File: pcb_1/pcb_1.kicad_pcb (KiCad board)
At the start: 2 copper layers, 46 parts, among them J1 ACin, J2 Vout, J3 2N3055_conn, J4 DCin, P1 CONN_01X07, P2 CONN_01X01, P3 CONN_01X01, P4 CONN_01X01, P5 CONN_01X01, P6 CONN_01X01, P7 CONN_01X01, Q2 BD139, U1 MAX9944ASA+T, U2 MCP3422A0-E/SN, U3 MCP4822-E/SN, U4 INA213AIDCKT, U5 LM7705MM/NOPB, U6 SPX2920U-5.0, U7 25V_regulator, U8 op_amp, U9 INA240A1PWR

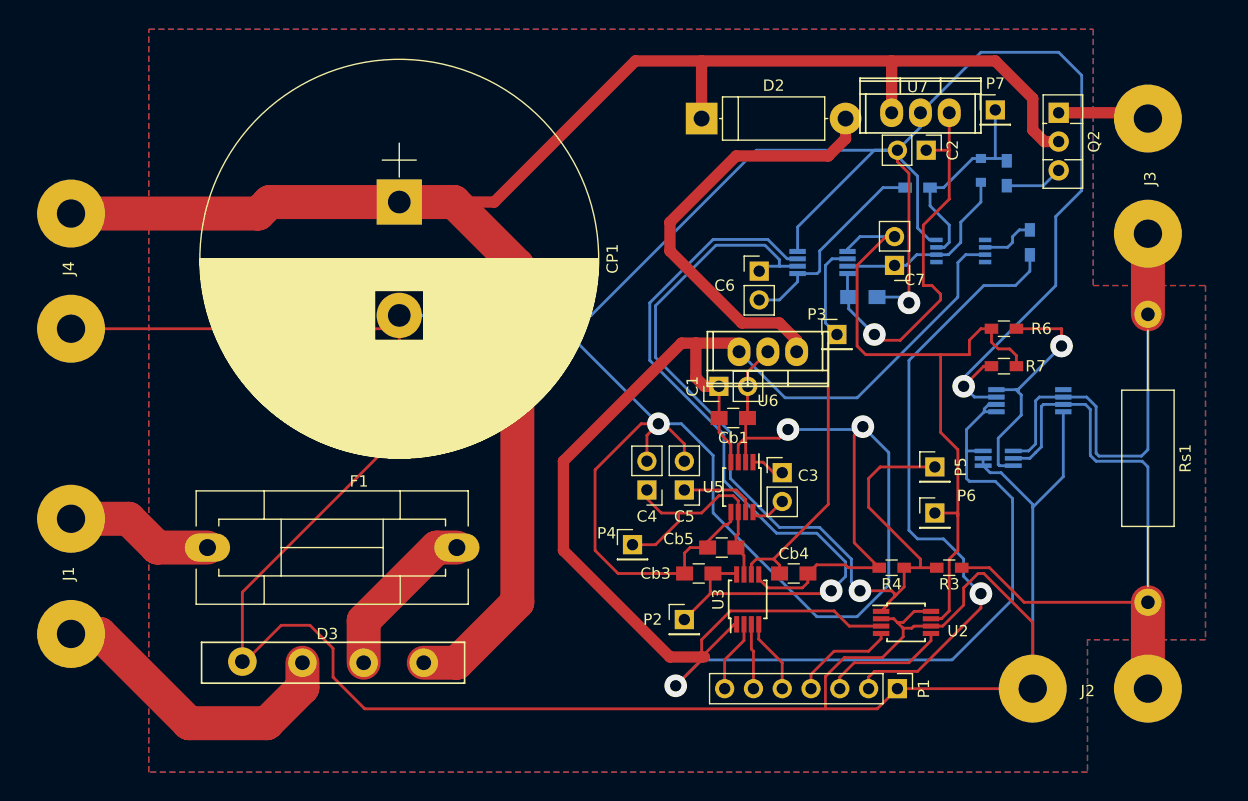
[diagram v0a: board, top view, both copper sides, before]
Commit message: Oparin regu vaihdettu ja konkkien footprintejä muutettu
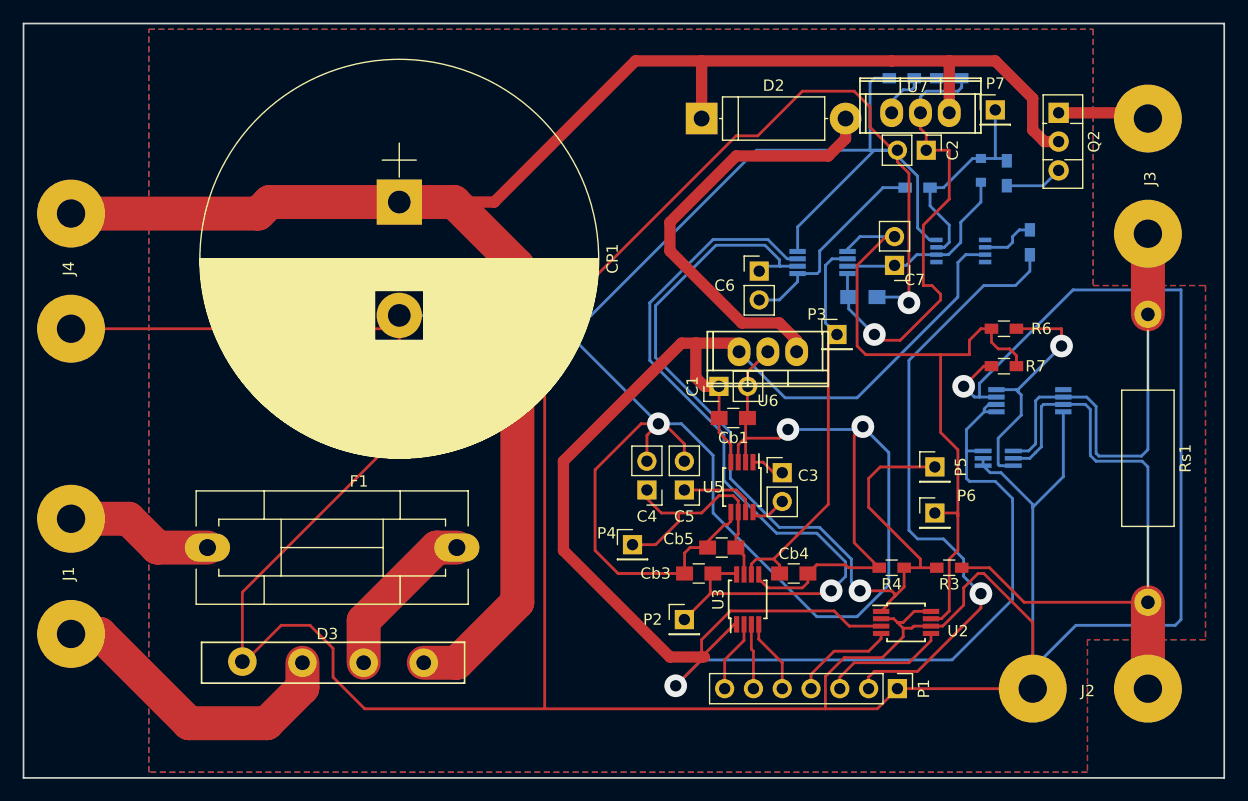
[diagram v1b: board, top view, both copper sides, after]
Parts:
- added R8: R, Resistors_SMD:R_0603_HandSoldering, B.Cu at (116.5, 33.0)
- added R9: R, Resistors_SMD:R_0603_HandSoldering, B.Cu at (120.7, 33.0)
- U7: value 25V_regulator -> LM317AT
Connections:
- U7 pad 1: Net-(CP1-Pad1) -> Net-(R8-Pad1)
- U7 pad 2: GND -> Net-(C2-Pad1)
- U7 pad 3: Net-(C2-Pad1) -> Net-(CP1-Pad1)
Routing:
- net GND: track 527.2 -> 627.0 mm
- net Net-(C2-Pad1): track 34.4 -> 40.9 mm
- net Net-(R8-Pad1): track 0.00 -> 6.31 mm
- net Net-(CP1-Pad1): track 155.8 -> 156.3 mm
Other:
- board outline added: 105.9 x 66.5 mm

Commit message: Traceja paksunnettu
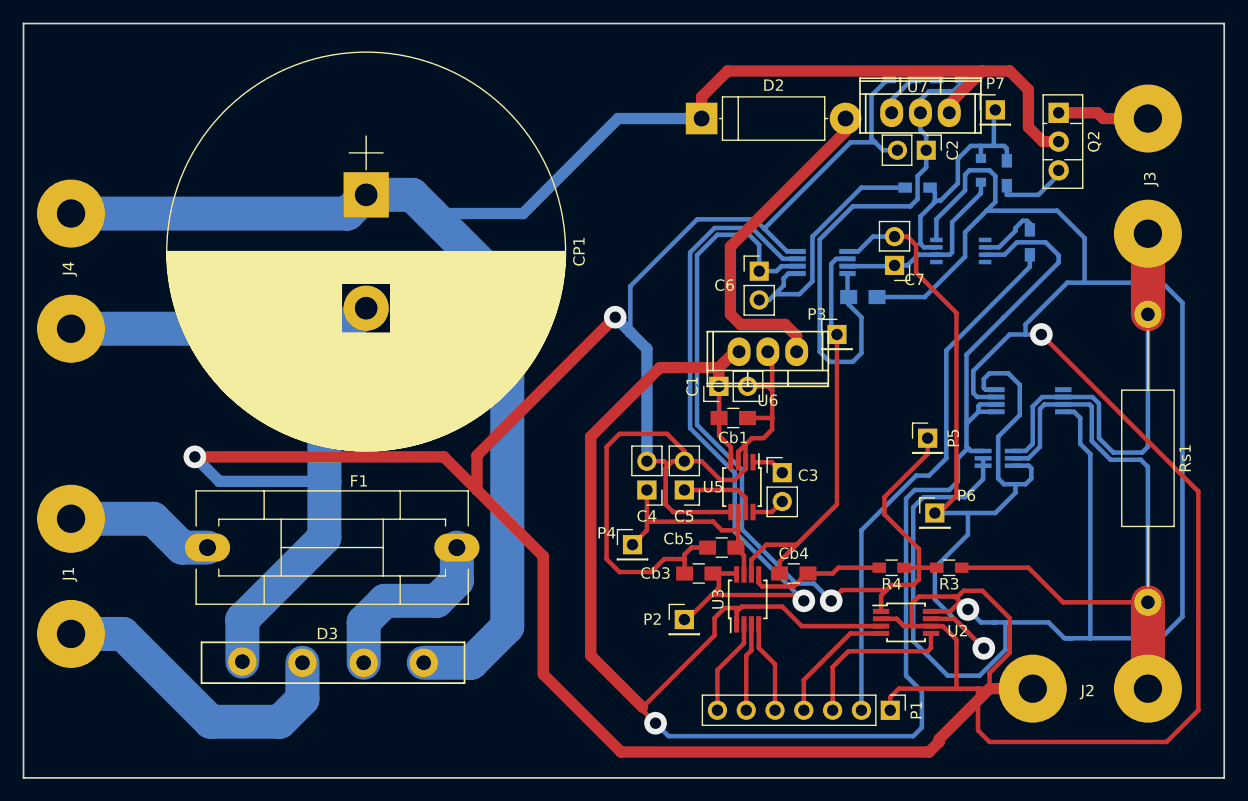
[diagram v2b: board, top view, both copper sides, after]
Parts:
- removed R6, R7: 10k, Resistors_SMD:R_0603_HandSoldering
- moved CP1 2.99 mm to (69.2, 43.3)
- moved P5 2.62 mm to (118.7, 64.8)
- moved P1 2.01 mm to (115.4, 88.8)
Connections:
- U4 pad 6: Net-(R6-Pad1) -> Net-(C7-Pad2)
- U9 pad 8: Net-(R6-Pad1) -> Net-(C7-Pad2)
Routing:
- net Net-(R6-Pad1): track 21.9 -> 0.00 mm, vias 1 -> 0
- net Net-(C7-Pad2): track 62.7 -> 83.0 mm, vias 0 -> 1
- net GND: track 627.0 -> 610.4 mm, vias 5 -> 4
- net Net-(D2-Pad2): track 38.3 -> 29.5 mm
- net current_limiter: track 55.1 -> 47.0 mm, vias 1 -> 0
- net Net-(Cb3-Pad1): track 69.2 -> 62.6 mm
- net Net-(C2-Pad1): track 40.9 -> 45.9 mm, vias 1 -> 0
- net Net-(CP1-Pad1): track 156.3 -> 152.1 mm
- net Net-(C6-Pad2): track 18.4 -> 22.4 mm
- net ADC_scl: track 11.0 -> 14.5 mm
- net Net-(D1-Pad2): track 19.1 -> 22.4 mm
- net -0.232V: track 22.7 -> 19.6 mm
- net DAC_cs: track 6.38 -> 8.55 mm
- net DAC_sck: track 5.75 -> 7.77 mm
- net +5V: track 170.7 -> 168.7 mm
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- removed copper zone on B.Cu, net GND
- removed copper zone on F.Cu, net GND

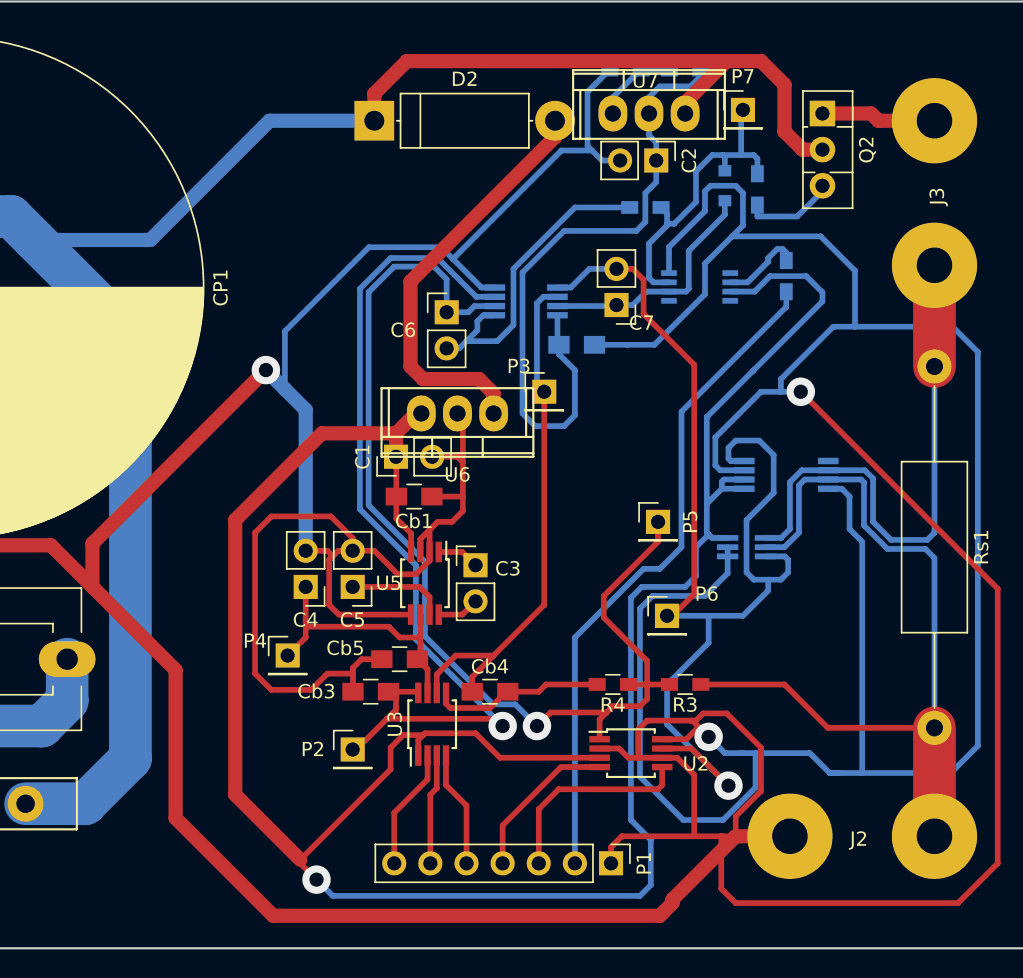
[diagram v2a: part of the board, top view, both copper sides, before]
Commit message: INA240 kotelo vaihdettu ja toinen vastaava vahvistin poistettu
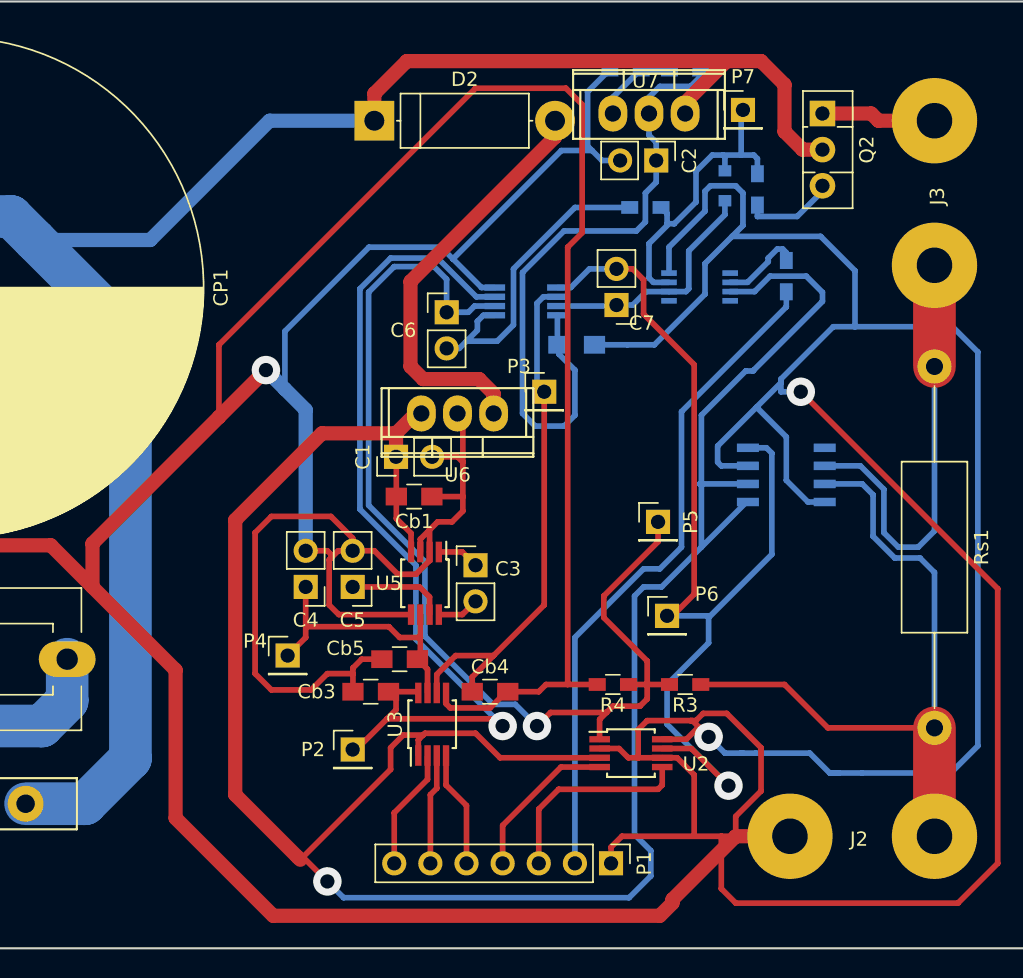
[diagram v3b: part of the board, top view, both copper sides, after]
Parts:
- removed U4: INA213AIDCKT, TO_SOT_Packages_SMD:SOT-363_SC-70-6_Handsoldering
- U9: footprint Housings_SSOP:TSSOP-8_4.4x3mm_Pitch0.65mm -> Housings_SOIC:SOIC-8_3.9x4.9mm_Pitch1.27mm
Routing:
- net GND: track 610.4 -> 643.9 mm
- net Net-(C7-Pad2): track 83.0 -> 71.9 mm
- net Net-(J2-Pad2): track 57.1 -> 48.2 mm
- net Net-(J3-Pad1): track 38.6 -> 31.0 mm

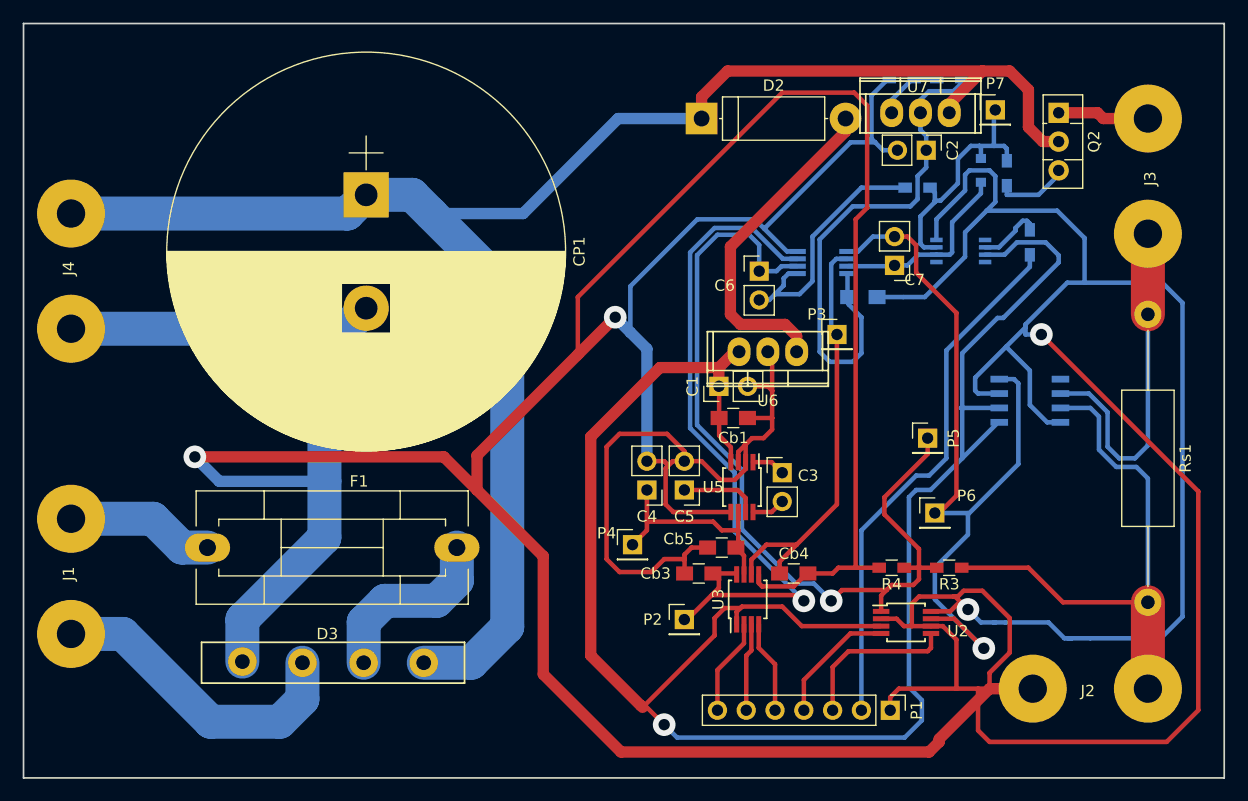
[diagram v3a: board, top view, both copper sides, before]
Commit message: Footprintteja muutettu oikeiksi
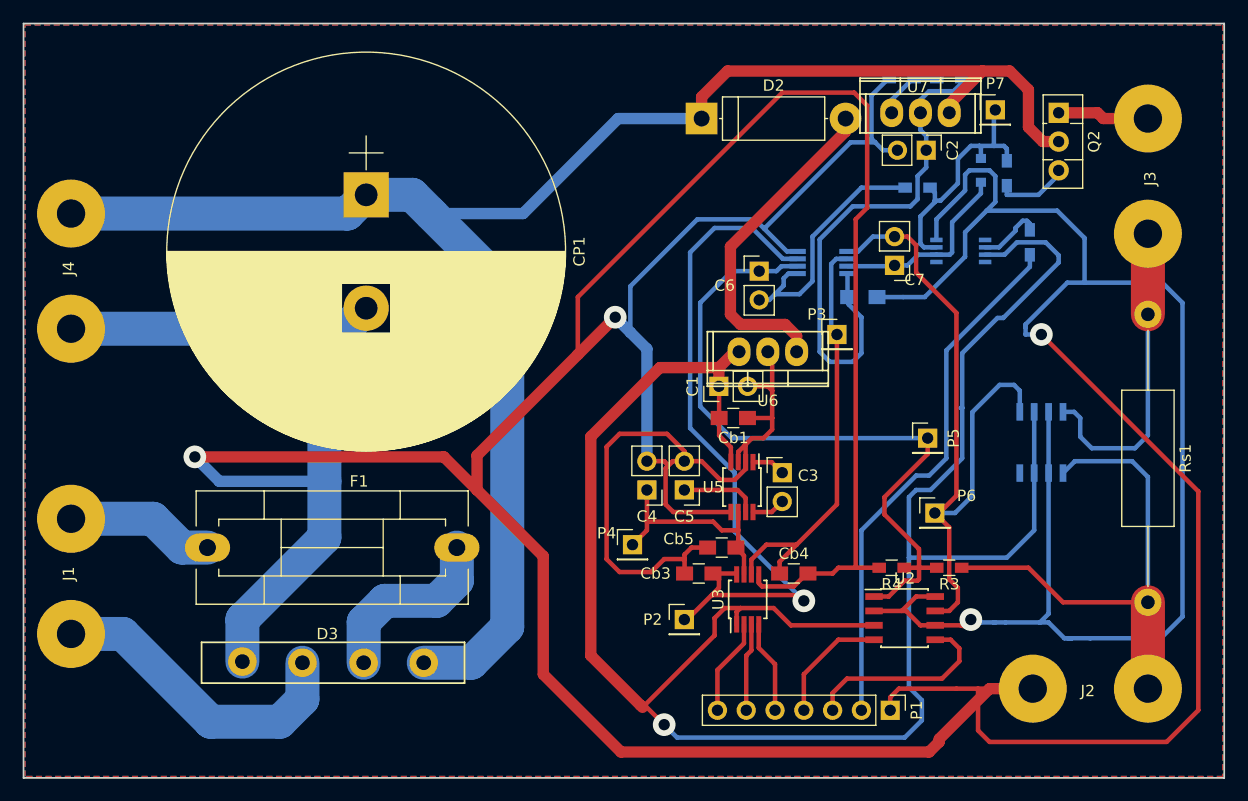
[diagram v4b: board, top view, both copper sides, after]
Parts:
- U2: footprint Housings_SSOP:MSOP-8_3x3mm_Pitch0.65mm -> Housings_SOIC:SOIC-8_3.9x4.9mm_Pitch1.27mm
- moved U9 3.82 mm to (128.8, 65.2), turned to 90 degrees
- moved U2 0.40 mm to (116.7, 80.6)
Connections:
- U9 pad 1: Net-(U9-Pad1) -> Net-(J2-Pad2)
- U9 pad 2: Net-(J3-Pad1) -> GND
- U9 pad 3: Net-(J2-Pad2) -> +5V
- U9 pad 4: GND -> Net-(U9-Pad4)
- U9 pad 5: +5V -> Net-(C7-Pad2)
- U9 pad 8: Net-(C7-Pad2) -> Net-(J3-Pad1)
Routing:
- net GND: track 643.9 -> 621.0 mm
- net Net-(C6-Pad1): track 77.6 -> 63.1 mm, vias 1 -> 0
- net +5V: track 168.9 -> 182.8 mm
- net Net-(C7-Pad2): track 71.9 -> 62.6 mm, vias 1 -> 0
- net Net-(J2-Pad2): track 48.2 -> 44.9 mm
- net ADC_scl: track 14.5 -> 17.4 mm
- net Net-(J3-Pad1): track 31.0 -> 28.0 mm
- net ADC_sda: track 11.2 -> 10.6 mm
- added copper zone on B.Cu, net GND
- added copper zone on F.Cu, net GND

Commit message: pcb:ssa nyt smd- ja tht-komponentit eri puolilla
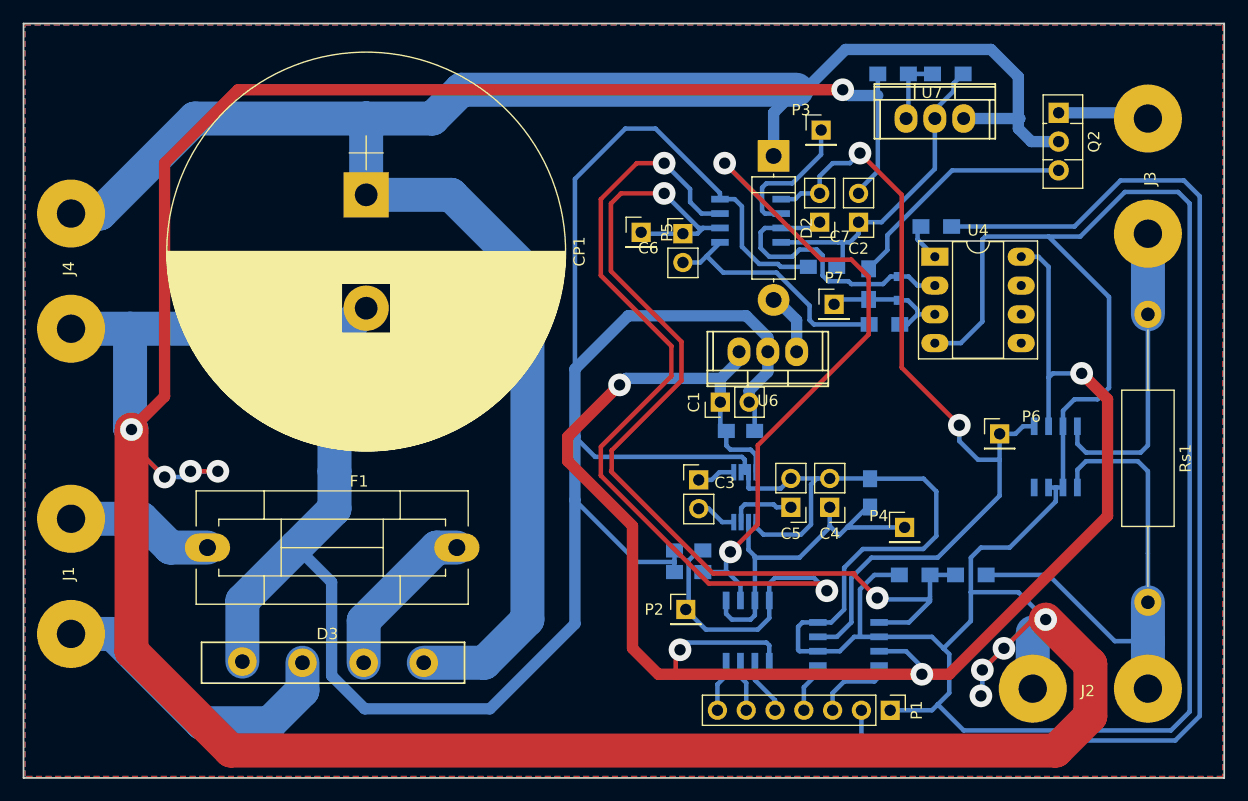
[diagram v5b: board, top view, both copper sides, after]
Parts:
- removed U8: op_amp, Housings_SSOP:TSSOP-8_3x3mm_Pitch0.65mm
- added U4: TL072, Housings_DIP:DIP-8_W7.62mm_Socket_LongPads, F.Cu at (119.4, 48.8)
- Cb1, Cb3, Cb4, Cb5, U2, U5: moved to B.Cu
- R1, R2, R5, R8, R9: footprint Resistors_SMD:R_0603_HandSoldering -> Resistors_SMD:R_0805_HandSoldering
- R3: footprint Resistors_SMD:R_0603_HandSoldering -> Resistors_SMD:R_0805_HandSoldering; moved to B.Cu
- R4: value 3.9k -> 1.2k; footprint Resistors_SMD:R_0603_HandSoldering -> Resistors_SMD:R_0805_HandSoldering; moved to B.Cu
- U1: footprint Housings_SSOP:MSOP-8_3x3mm_Pitch0.65mm -> Housings_SOIC:SOIC-8_3.9x4.9mm_Pitch1.27mm
- U3: footprint Housings_SSOP:MSOP-8_3x3mm_Pitch0.65mm -> Housings_SOIC:SOIC-8_3.9x4.9mm_Pitch1.27mm; moved to B.Cu
- moved P5 31.1 mm to (93.5, 46.6)
- moved P4 24.1 mm to (116.7, 72.6)
- moved P7 22.3 mm to (110.5, 53.0)
- moved P3 18.1 mm to (109.3, 37.6)
- moved C4 16.2 mm to (110.1, 70.9)
- moved R2 15.6 mm to (113.5, 51.2), turned to 270 degrees
- moved Cb5 13.9 mm to (113.7, 69.6), turned to 90 degrees
- moved D1 12.7 mm to (116.2, 51.6), turned to 270 degrees
- moved R1 12.4 mm to (114.9, 54.7)
- moved C5 9.52 mm to (106.7, 70.9)
- moved Cb4 9.27 mm to (97.7, 76.6), turned to 180 degrees
- moved P6 9.03 mm to (125.1, 64.4)
- moved C2 8.72 mm to (112.6, 45.7), turned to 180 degrees
- moved R5 8.37 mm to (119.5, 46.1), turned to 0 degrees
- moved C7 7.62 mm to (109.2, 45.7)
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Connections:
- P1 pad 3: ADC_scl -> ADC_sda
- P1 pad 4: ADC_sda -> ADC_scl
- P1 pad 5: DAC_sdi -> DAC_cs
- P1 pad 7: DAC_cs -> DAC_sdi
- U3 pad 5: GND -> -0.232V
- U9 pad 3: +5V -> GND
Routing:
- net GND: track 621.0 -> 737.8 mm, vias 4 -> 9
- net current_limiter: track 47.0 -> 103.1 mm
- net Net-(Cb4-Pad1): track 37.1 -> 70.5 mm, vias 0 -> 2
- net +5V: track 182.8 -> 149.4 mm, vias 1 -> 4
- net Net-(Cb3-Pad1): track 62.6 -> 91.4 mm, vias 1 -> 2
- net Net-(C6-Pad1): track 63.1 -> 88.7 mm, vias 0 -> 2
- net Net-(CP1-Pad1): track 152.1 -> 176.1 mm
- net Net-(D2-Pad2): track 29.5 -> 5.56 mm
- net Net-(C2-Pad1): track 45.9 -> 28.6 mm
- net Net-(Q2-Pad3): track 6.49 -> 21.1 mm
- net ADC_scl: track 17.4 -> 4.45 mm
- net -0.232V: track 19.6 -> 32.3 mm
- net Net-(C7-Pad2): track 62.6 -> 75.1 mm, vias 0 -> 2
- net Net-(D1-Pad2): track 22.4 -> 12.0 mm
- net Net-(C7-Pad1): track 17.0 -> 25.8 mm
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
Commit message: 30.10 syövytetty pcb
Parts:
- added R6: R, Resistors_SMD:R_0805_HandSoldering, B.Cu at (109.7, 75.3)
- added R7: R, Resistors_SMD:R_0805_HandSoldering, B.Cu at (104.9, 75.3)
- moved P4 1.17 mm to (117.0, 71.5)
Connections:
- Cb5 pad 1: -0.232V -> Net-(Cb5-Pad1)
- P4 pad 1: -0.232V -> Net-(Cb5-Pad1)
- U1 pad 5: Net-(C7-Pad2) -> Net-(Cb4-Pad1)
- U1 pad 6: Net-(Cb4-Pad1) -> Net-(C7-Pad2)
- U3 pad 5: -0.232V -> Net-(Cb5-Pad1)
- U3 pad 7: -0.232V -> Net-(Cb5-Pad1)
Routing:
- net Net-(Cb5-Pad1): track 0.00 -> 26.0 mm
- net -0.232V: track 32.3 -> 12.2 mm
- net GND: track 737.8 -> 739.2 mm
- net Net-(Cb4-Pad1): track 70.5 -> 69.6 mm
- net Net-(C7-Pad2): track 75.1 -> 75.8 mm
